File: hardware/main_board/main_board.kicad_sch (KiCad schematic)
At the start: 58 parts, among them J1 FFC_Prog_Conn, Q1 TP0610T, SW1 PTS810SJG250SMTR LFS, SW2 PTS810SJG250SMTR LFS, SW3 PTS810SJG250SMTR LFS, SW4 PTS810SJG250SMTR LFS, SW5 PTS810SJG250SMTR LFS, SW6 PTS810SJG250SMTR LFS, U1 BT840F, U2 LP5813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

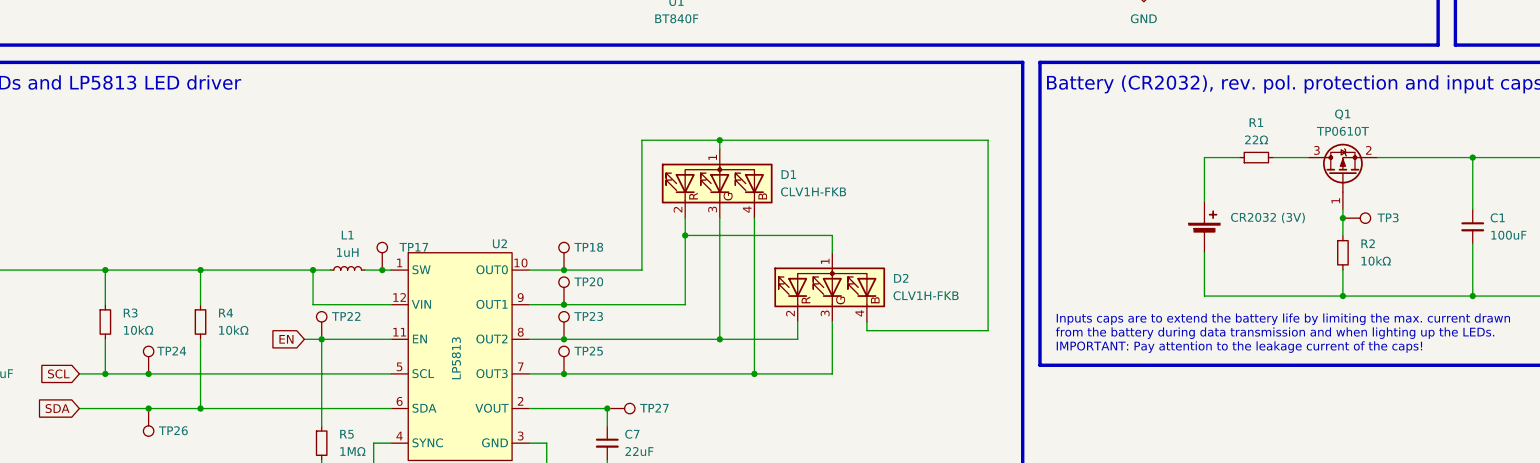
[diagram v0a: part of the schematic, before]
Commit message: Changed LEDs module to use FIFO and got UART for logging working
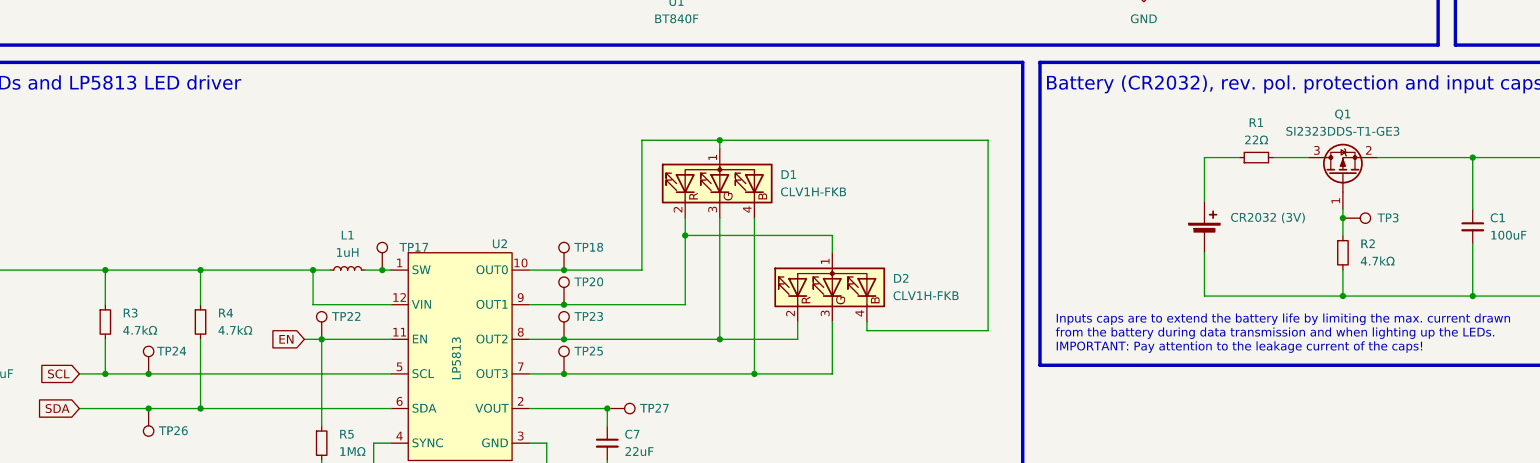
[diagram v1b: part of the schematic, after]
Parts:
- Q1: value TP0610T -> SI2323DDS-T1-GE3
- R2, R3, R4: value 10kΩ -> 4.7kΩ; symbol KiPLM:RES/RES-0000-0103 -> KiPLM:RES/RES-0000-0473; IPN RES-0000-0103 -> RES-0000-0473; MPN CRCW060310K0FKEAC -> CRCW06034K70FKEAC; Mouser-PN 71-CRCW060310K0FKEAC -> 71-CRCW06034K70FKEAC; Resistance 10kΩ -> 4.7kΩ; Temperature Coefficient 100 PPM/°C -> 100PPM/°C
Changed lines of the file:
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@@
 	)
 	(symbol
-		(lib_id "KiPLM:RES/RES-0000-0103")
+		(lib_id "KiPLM:RES/RES-0000-0473")
 		(at 222.25 147.32 0)
 		(unit 1)
@@
 			)
 		)
-		(property "Value" "10kΩ"
+		(property "Value" "4.7kΩ"
 			(at 223.012 148.336 0)
 			(effects
@@
 			)
 		)
-		(property "Description" "Thick Film Resistors - SMD 1/10Watt 10Kohms 1% Commercial Use"
+		(property "Description" "Thick Film Resistors - SMD 1/10Watt 4.7Kohms 1% Commercial Use"
 			(at 222.25 147.32 0)
 			(effects
@@
 			)
 		)
-		(property "Resistance" "10kΩ"
+		(property "Resistance" "4.7kΩ"
 			(at 224.79 148.5899 0)
 			(effects
@@
 			)
 		)
-		(property "IPN" "RES-0000-0103"
+		(property "IPN" "RES-0000-0473"
 			(at 222.25 147.32 0)
 			(effects
@@
 			)
 		)
-		(property "MPN" "CRCW060310K0FKEAC"
+		(property "MPN" "CRCW06034K70FKEAC"
 			(at 222.25 147.32 0)
 			(effects
@@
 			)
 		)
-		(property "Temperature Coefficient" "100 PPM/°C"
+		(property "Temperature Coefficient" "100PPM/°C"
 			(at 222.25 147.32 0)
 			(effects
@@
 			)
 		)
-		(property "Mouser-PN" "71-CRCW060310K0FKEAC"
+		(property "Mouser-PN" "71-CRCW06034K70FKEAC"
 			(at 222.25 147.32 0)
 			(effects
@@
 			)
 		)
-		(property "Value" "TP0610T"
+		(property "Value" "SI2323DDS-T1-GE3"
 			(at 222.25 129.54 90)
 			(effects
@@
 	)
 	(symbol
-		(lib_id "KiPLM:RES/RES-0000-0103")
+		(lib_id "KiPLM:RES/RES-0000-0473")
 		(at 40.64 157.48 0)
 		(unit 1)
@@
 			)
 		)
-		(property "Value" "10kΩ"
+		(property "Value" "4.7kΩ"
 			(at 41.402 158.496 0)
 			(effects
@@
 			)
 		)
-		(property "Description" "Thick Film Resistors - SMD 1/10Watt 10Kohms 1% Commercial Use"
+		(property "Description" "Thick Film Resistors - SMD 1/10Watt 4.7Kohms 1% Commercial Use"
 			(at 40.64 157.48 0)
 			(effects
@@
 			)
 		)
-		(property "Resistance" "10kΩ"
+		(property "Resistance" "4.7kΩ"
 			(at 43.18 158.7499 0)
 			(effects
@@
 			)
 		)
-		(property "IPN" "RES-0000-0103"
+		(property "IPN" "RES-0000-0473"
 			(at 40.64 157.48 0)
 			(effects
@@
 			)
 		)
-		(property "MPN" "CRCW060310K0FKEAC"
+		(property "MPN" "CRCW06034K70FKEAC"
 			(at 40.64 157.48 0)
 			(effects
@@
 			)
 		)
-		(property "Temperature Coefficient" "100 PPM/°C"
+		(property "Temperature Coefficient" "100PPM/°C"
 			(at 40.64 157.48 0)
 			(effects
@@
 			)
 		)
-		(property "Mouser-PN" "71-CRCW060310K0FKEAC"
+		(property "Mouser-PN" "71-CRCW06034K70FKEAC"
 			(at 40.64 157.48 0)
 			(effects
@@
 	)
 	(symbol
-		(lib_id "KiPLM:RES/RES-0000-0103")
+		(lib_id "KiPLM:RES/RES-0000-0473")
 		(at 54.61 157.48 0)
 		(unit 1)
@@
 			)
 		)
-		(property "Value" "10kΩ"
+		(property "Value" "4.7kΩ"
 			(at 55.372 158.496 0)
 			(effects
@@
 			)
 		)
-		(property "Description" "Thick Film Resistors - SMD 1/10Watt 10Kohms 1% Commercial Use"
+		(property "Description" "Thick Film Resistors - SMD 1/10Watt 4.7Kohms 1% Commercial Use"
 			(at 54.61 157.48 0)
 			(effects
@@
 			)
 		)
-		(property "Resistance" "10kΩ"
+		(property "Resistance" "4.7kΩ"
 			(at 57.15 158.7499 0)
 			(effects
@@
 			)
 		)
-		(property "IPN" "RES-0000-0103"
+		(property "IPN" "RES-0000-0473"
 			(at 54.61 157.48 0)
 			(effects
@@
 			)
 		)
-		(property "MPN" "CRCW060310K0FKEAC"
+		(property "MPN" "CRCW06034K70FKEAC"
 			(at 54.61 157.48 0)
 			(effects
@@
 			)
 		)
-		(property "Temperature Coefficient" "100 PPM/°C"
+		(property "Temperature Coefficient" "100PPM/°C"
 			(at 54.61 157.48 0)
 			(effects
@@
 			)
 		)
-		(property "Mouser-PN" "71-CRCW060310K0FKEAC"
+		(property "Mouser-PN" "71-CRCW06034K70FKEAC"
 			(at 54.61 157.48 0)
 			(effects
